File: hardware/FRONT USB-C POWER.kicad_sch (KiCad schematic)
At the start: 0 parts

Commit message: working on adujustabel otpur for usbpd
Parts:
- added C20: CIN, symbol Device:C
- added C21, C22: 2uF2, symbol Device:C
- added C23, C24, C27, C28, C29, C30, C33: C, symbol Device:C
- added C25: COUT2, symbol Device:C
- added C26: COUT1, symbol Device:C
- added C31, C32: 1uF, symbol Device:C
- added C34: 470nF, symbol Device:C
- added D2, D3: D_Shockley, symbol Device:D_Shockley
- added L3, L4: L, symbol Device:L
- added Q3, Q4, Q5, Q6: Q_NMOS_GDS, symbol Device:Q_NMOS_GDS
- added R13: RHO1, symbol Device:R
- added R14: RHO2, symbol Device:R
- added R15, R16, R17, R18: R, symbol Device:R
- added R19: 10K, symbol Device:R
- added R21, R22: 100K, symbol Device:R
- added R23: 470R, symbol Device:R
- added Uw: ~, symbol CARTHING:LM5143-Q1
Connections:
- new net: C21.1, C22.1, D2.2 (A), D3.2 (A), Uw.15 (VCC), Uw.16 (VCC)
- new net: C32.2, Uw.1 (SS2)
- new net: C24.2, L3.1, Q5.3 (S), Q6.2 (D), Uw.10 (SW2)
- new net: C24.1, D3.1 (K), Uw.11 (HB2)
- new net: Q6.1 (G), Uw.12 (LOL2), Uw.13 (LO2)
- new net: Q4.1 (G), Uw.18 (LO1), Uw.19 (LOL1)
- new net: C30.1, R17.1, Uw.2 (COMP2)
- new net: C23.2, D2.1 (K), Uw.20 (HB1)
- new net: C23.1, L4.2, Q3.3 (S), Q4.2 (D), Uw.21 (SW1)
- new net: R13.2, Uw.22 (HO1)
- new net: Q3.1 (G), R13.1, Uw.23 (HOL1)
- new net: L4.1, R15.2, Uw.27 (CS1)
- new net: C28.2, R18.2, Uw.29 (COMP1)
- new net: C31.2, Uw.30 (SS1)
- new net: C33.2, Uw.32 (RES)
- new net: C34.2, Uw.36 (VDDA), Uw.38 (DITH)
- new net: R19.1, Uw.37 (RT)
- new net: L3.2, R16.1, Uw.4 (CS2)
- new net: Q5.1 (G), R14.2, Uw.8 (HOL2)
- new net: R14.1, Uw.9 (HO2)
- new net: C29.1, R17.2
- new net: R19.2, R23.1
- new net: C27.2, R18.1
- new net +21V: C20.2, Q3.2 (D), Q5.2 (D), Uw.25 (VIN)
- new net +3V3: R21.2, R22.1
- new net +5V: Uw.6 (VCCX)
- new net B_SUB-C_BUCK_P-GOOD: R21.1, Uw.7 (PG2)
- new net B_USB-C_BUCK_EN: Uw.40 (EN2)
- new net B_USB-C_BUCK_FB: Uw.3 (FB2)
- new net B_USB-C_BUCK_OUT: C25.1, R16.2, Uw.5 (VOUT2)
- new net F_SUB-C_BUCK_P-GOOD: R22.2, Uw.24 (PG1)
- new net F_USB-C_BUCK_EN: Uw.31 (EN1)
- new net F_USB-C_BUCK_FB: Uw.28 (FB1)
- new net F_USB-C_BUCK_OUT: C26.1, R15.1, Uw.26 (VOUT1)
- new net GND: C20.1, C21.2, C22.2, C25.2, C26.2, C27.1, C28.1, C29.2, C30.2, C31.1, C32.1, C33.1, C34.1, Q4.3 (S), Q6.3 (S), R23.2, Uw.14 (PGND2), Uw.17 (PGND1), Uw.35 (AGND), Uw.EP
- new net USB-C_BUCK_CLK_IN: Uw.33 (DEMB)
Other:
- added sheet F_AND_B_VOUT_FEEDBACK_NETWORKS (F_AND_B_VOUT_FEEDBACK_NETWORKS.kicad_sch)
- note added: "2.1 MHz SW FREQ"
- note added: "CANT LEVE EN PINS FLOATING"

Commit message: making hardware progress
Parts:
- removed L3, L4: L, symbol Device:L
- added L1 (x2): IHLP2525CZER2R2M01, symbol Device:L
- added R51: 0R, symbol Device:R
- C20: renamed from C26; value COUT1 -> 4.7uF
- C21: renamed from C27; value C -> 4.7uF
- C22: renamed from C28; value C -> 18pF
- C24: renamed from C33; value C -> 470nF
- C25: renamed from C23; value C -> 0.1uF
- C26: renamed from C20; value CIN -> 50uF
- C30: renamed from C24; value C -> 0.1uF
- C32: renamed from C30; value C -> 18pF
- C33: renamed from C29; value C -> 4.7uF
- C34: renamed from C25; value COUT2 -> 4.7uF
- Q3, Q4, Q5, Q6: value Q_NMOS_GDS -> PMPB11EN,115
- R14: renamed from R18; value R -> 5.9K
- R15: value R -> 10mR
- R22: renamed from R16; value R -> 10mR
- R23: renamed from R17; value R -> 5.9K
- renumbered C31 to C23, C22 to C27, C34 to C28, C21 to C29, C32 to C31, R22 to R16, R13 to R17, R19 to R18, R14 to R19, R23 to R20, Uw to U6
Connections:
- net GND: now also U6.34 (MODE), R51.2
- net USB-C_BUCK_CLK_IN: now also R51.1
- net at C30.2, Q5.3 (S), Q6.2 (D)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: now also L1.1
- net at C25.1, Q3.3 (S), Q4.2 (D)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: now also L1.2
- net F_USB-C_CSN: now reaches R15.2, U6.27 (CS1)
- net F_USB-C_CSN: now also L1.1
- net B_USB-C_CSN: now reaches R22.1, U6.4 (CS2)
- net B_USB-C_CSN: now also L1.2
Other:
- note added: "2.2uH"
- moved on the sheet: C25, D2

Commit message: working on hardware
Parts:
- C24: renamed from C20; footprint (none) -> Capacitor_SMD:C_0603_1608Metric
- C25: renamed from C21; footprint (none) -> Capacitor_SMD:C_0603_1608Metric
- C26: renamed from C22; footprint (none) -> Capacitor_SMD:C_0603_1608Metric
- C27: renamed from C23; footprint (none) -> Capacitor_SMD:C_0603_1608Metric
- C28: renamed from C24; footprint (none) -> Capacitor_SMD:C_0805_2012Metric
- C29: renamed from C25; footprint (none) -> Capacitor_SMD:C_0603_1608Metric
- C30: renamed from C26; footprint (none) -> Capacitor_SMD:C_0603_1608Metric
- C31: renamed from C27; value 2uF2 -> 2.2uF; footprint (none) -> Capacitor_SMD:C_0603_1608Metric
- C32: renamed from C28; footprint (none) -> Capacitor_SMD:C_0805_2012Metric
- C33: renamed from C29; value 2uF2 -> 2.2uF; footprint (none) -> Capacitor_SMD:C_0603_1608Metric
- C34: renamed from C30; footprint (none) -> Capacitor_SMD:C_0603_1608Metric
- C35: renamed from C31; footprint (none) -> Capacitor_SMD:C_0603_1608Metric
- C36: renamed from C32; footprint (none) -> Capacitor_SMD:C_0603_1608Metric
- C37: renamed from C33; footprint (none) -> Capacitor_SMD:C_0603_1608Metric
- C38: renamed from C34; footprint (none) -> Capacitor_SMD:C_0603_1608Metric
- D3: renamed from D2; footprint (none) -> Diode_SMD:D_SMA
- D4: renamed from D3; footprint (none) -> Diode_SMD:D_SMA
- Q3, Q4, Q5, Q6: footprint (none) -> CARTHING:TRANS_PMPB11EN_115
- renumbered R14 to R17, R15 to R18, R16 to R19, R17 to R20, R51 to R21, R18 to R22, R19 to R23, R20 to R24, R21 to R25, R22 to R26, R23 to R27, U6 to U7

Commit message: working assighning footprints still
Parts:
- added TP8: TestPoint, TestPoint:TestPoint_Pad_D1.0mm, symbol Connector:TestPoint
- R17, R19, R20, R21, R22, R23, R24, R25, R27: footprint (none) -> Resistor_SMD:R_0603_1608Metric
- R18, R26: footprint (none) -> Resistor_SMD:R_1206_3216Metric
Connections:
- net at U7.39 (SYNCOUT): now also TP8.1
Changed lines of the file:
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@@
     (stroke (width 0) (type default))
   )
-  (wire (pts (xy 163.83 119.38) (xy 163.83 135.89))
+  (wire (pts (xy 170.18 119.38) (xy 170.18 135.89))
     (stroke (width 0) (type default))
   )
@@
     (stroke (width 0) (type default))
   )
-  (wire (pts (xy 158.75 119.38) (xy 163.83 119.38))
+  (wire (pts (xy 158.75 119.38) (xy 170.18 119.38))
     (stroke (width 0) (type default))
   )
@@
     (stroke (width 0) (type default))
   )
-  (wire (pts (xy 163.83 135.89) (xy 143.51 135.89))
+  (wire (pts (xy 143.51 135.89) (xy 170.18 135.89))
     (stroke (width 0) (type default))
   )
@@
     (stroke (width 0) (type default))
   )
-  (text "2.1 MHz SW FREQ\n" (at 166.37 137.16 0)
+  (text "2.1 MHz SW FREQ\n" (at 172.72 137.16 0)
     (effects (font (size 1.27 1.27)) (justify left bottom))
   )
@@
       (effects (font (size 1.27 1.27)))
     )
-    (property "Footprint" "" (at 224.79 107.188 90)
+    (property "Footprint" "Resistor_SMD:R_0603_1608Metric" (at 224.79 107.188 90)
       (effects (font (size 1.27 1.27)) hide)
     )
@@
       (effects (font (size 1.27 1.27)))
     )
-    (property "Footprint" "" (at 58.42 74.168 90)
+    (property "Footprint" "Resistor_SMD:R_1206_3216Metric" (at 58.42 74.168 90)
       (effects (font (size 1.27 1.27)) hide)
     )
@@
       (effects (font (size 1.27 1.27)))
     )
-    (property "Footprint" "" (at 115.57 131.318 90)
+    (property "Footprint" "Resistor_SMD:R_0603_1608Metric" (at 115.57 131.318 90)
       (effects (font (size 1.27 1.27)) hide)
     )
@@
       (effects (font (size 1.27 1.27)))
     )
-    (property "Footprint" "" (at 223.52 75.438 90)
+    (property "Footprint" "Resistor_SMD:R_1206_3216Metric" (at 223.52 75.438 90)
       (effects (font (size 1.27 1.27)) hide)
     )
@@
     )
   )
+  (symbol (lib_id "Connector:TestPoint") (at 158.75 121.92 180) (unit 1)
+    (in_bom yes) (on_board yes) (dnp no) (fields_autoplaced)
+    (property "Reference" "TP8" (at 160.147 124.5783 0)
+      (effects (font (size 1.27 1.27)) (justify right))
+    )
+    (property "Value" "TestPoint" (at 160.147 126.4993 0)
+      (effects (font (size 1.27 1.27)) (justify right))
+    )
+    (property "Footprint" "TestPoint:TestPoint_Pad_D1.0mm" (at 153.67 121.92 0)
+      (effects (font (size 1.27 1.27)) hide)
+    )
+    (property "Datasheet" "~" (at 153.67 121.92 0)
+      (effects (font (size 1.27 1.27)) hide)
+    )
+    (pin "1")
+    (instances
+      (project "usbc-car-module"
+        (path "/fae025e9-99c5-40c1-af6f-99dc1edbfa43/91b561d6-4186-4f6f-8a2c-57c2c305f210"
+          (reference "TP8") (unit 1)
+        )
+      )
+    )
+  )
   (symbol (lib_id "Device:R") (at 204.47 114.3 90) (unit 1)
     (in_bom yes) (on_board yes) (dnp no) (fields_autoplaced)
@@
       (effects (font (size 1.27 1.27)))
     )
-    (property "Footprint" "" (at 204.47 116.078 90)
+    (property "Footprint" "Resistor_SMD:R_0603_1608Metric" (at 204.47 116.078 90)
       (effects (font (size 1.27 1.27)) hide)
     )
@@
       (effects (font (size 1.27 1.27)))
     )
-    (property "Footprint" "" (at 168.91 72.898 90)
+    (property "Footprint" "Resistor_SMD:R_0603_1608Metric" (at 168.91 72.898 90)
       (effects (font (size 1.27 1.27)) hide)
     )
@@
       (effects (font (size 1.27 1.27)))
     )
-    (property "Footprint" "" (at 111.76 72.898 90)
+    (property "Footprint" "Resistor_SMD:R_0603_1608Metric" (at 111.76 72.898 90)
       (effects (font (size 1.27 1.27)) hide)
     )
@@
       (effects (font (size 1.27 1.27)))
     )
-    (property "Footprint" "" (at 165.1 118.618 90)
+    (property "Footprint" "Resistor_SMD:R_0603_1608Metric" (at 165.1 118.618 90)
       (effects (font (size 1.27 1.27)) hide)
     )
@@
       (effects (font (size 1.27 1.27)))
     )
-    (property "Footprint" "" (at 173.99 118.618 90)
+    (property "Footprint" "Resistor_SMD:R_0603_1608Metric" (at 173.99 118.618 90)
       (effects (font (size 1.27 1.27)) hide)
     )
@@
       (effects (font (size 1.27 1.27)))
     )
-    (property "Footprint" "" (at 57.15 108.458 90)
+    (property "Footprint" "Resistor_SMD:R_0603_1608Metric" (at 57.15 108.458 90)
       (effects (font (size 1.27 1.27)) hide)
     )
@@
       (effects (font (size 1.27 1.27)))
     )
-    (property "Footprint" "" (at 78.74 116.078 90)
-      (effects (font (size 1.27 1.27)) hide)
-    )
+    (property "Footprint" "Resistor_SMD:R_0603_1608Metric" (at 78.74 116.078 90)
+      (effects (font (size 1.27 1.27)) hide)
+    )

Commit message: FINALY starting the pcb
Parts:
- L1: footprint (none) -> CARTHING:IND25X25CZ
- U7: footprint (none) -> CARTHING:LM5143
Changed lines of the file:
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@@
       (effects (font (size 1.27 1.27)))
     )
-    (property "Footprint" "" (at 149.86 76.2 0)
+    (property "Footprint" "CARTHING:LM5143" (at 149.86 76.2 0)
       (effects (font (size 1.27 1.27)) hide)
     )
@@
       (effects (font (size 1.27 1.27)))
     )
-    (property "Footprint" "" (at 210.82 73.66 0)
+    (property "Footprint" "CARTHING:IND25X25CZ" (at 210.82 73.66 0)
       (effects (font (size 1.27 1.27)) hide)
     )
@@
       (effects (font (size 1.27 1.27)))
     )
-    (property "Footprint" "" (at 71.12 72.39 0)
-      (effects (font (size 1.27 1.27)) hide)
-    )
+    (property "Footprint" "CARTHING:IND25X25CZ" (at 71.12 72.39 0)
+      (effects (font (size 1.27 1.27)) hide)
+    )

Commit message: coldent sleep so came back and did somre routing
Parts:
- R20, R23: now not fitted
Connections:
- net +21V: now also Q3.1 (D), Q3.5 (D), Q3.6 (D), Q3.7 (D), Q5.1 (D), Q5.5 (D), Q5.6 (D), Q5.7 (D)
- net GND: now also Q4.4 (S), Q4.8 (S), Q6.4 (S), Q6.8 (S), U7.41 (EP); no longer Q4.3 (S), Q6.3 (S), U7.EP
- net at C34.2, L1.1, Q6.2 (D)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: now also Q5.4 (S), Q5.8 (S), Q6.1 (D), Q6.5 (D), Q6.6 (D), Q6.7 (D); no longer Q5.3 (S)
- net at U7.12 (LOL2), U7.13 (LO2): now also Q6.3 (G); no longer Q6.1 (G)
- net at U7.18 (LO1), U7.19 (LOL1): now also Q4.3 (G); no longer Q4.1 (G)
- net at C29.1, L1.2, Q4.2 (D)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: now also Q3.4 (S), Q3.8 (S), Q4.1 (D), Q4.5 (D), Q4.6 (D), Q4.7 (D); no longer Q3.3 (S)
- net at R20.1, U7.23 (HOL1): now also Q3.3 (G); no longer Q3.1 (G)
- net at R23.2, U7.8 (HOL2): now also Q5.3 (G); no longer Q5.1 (G)

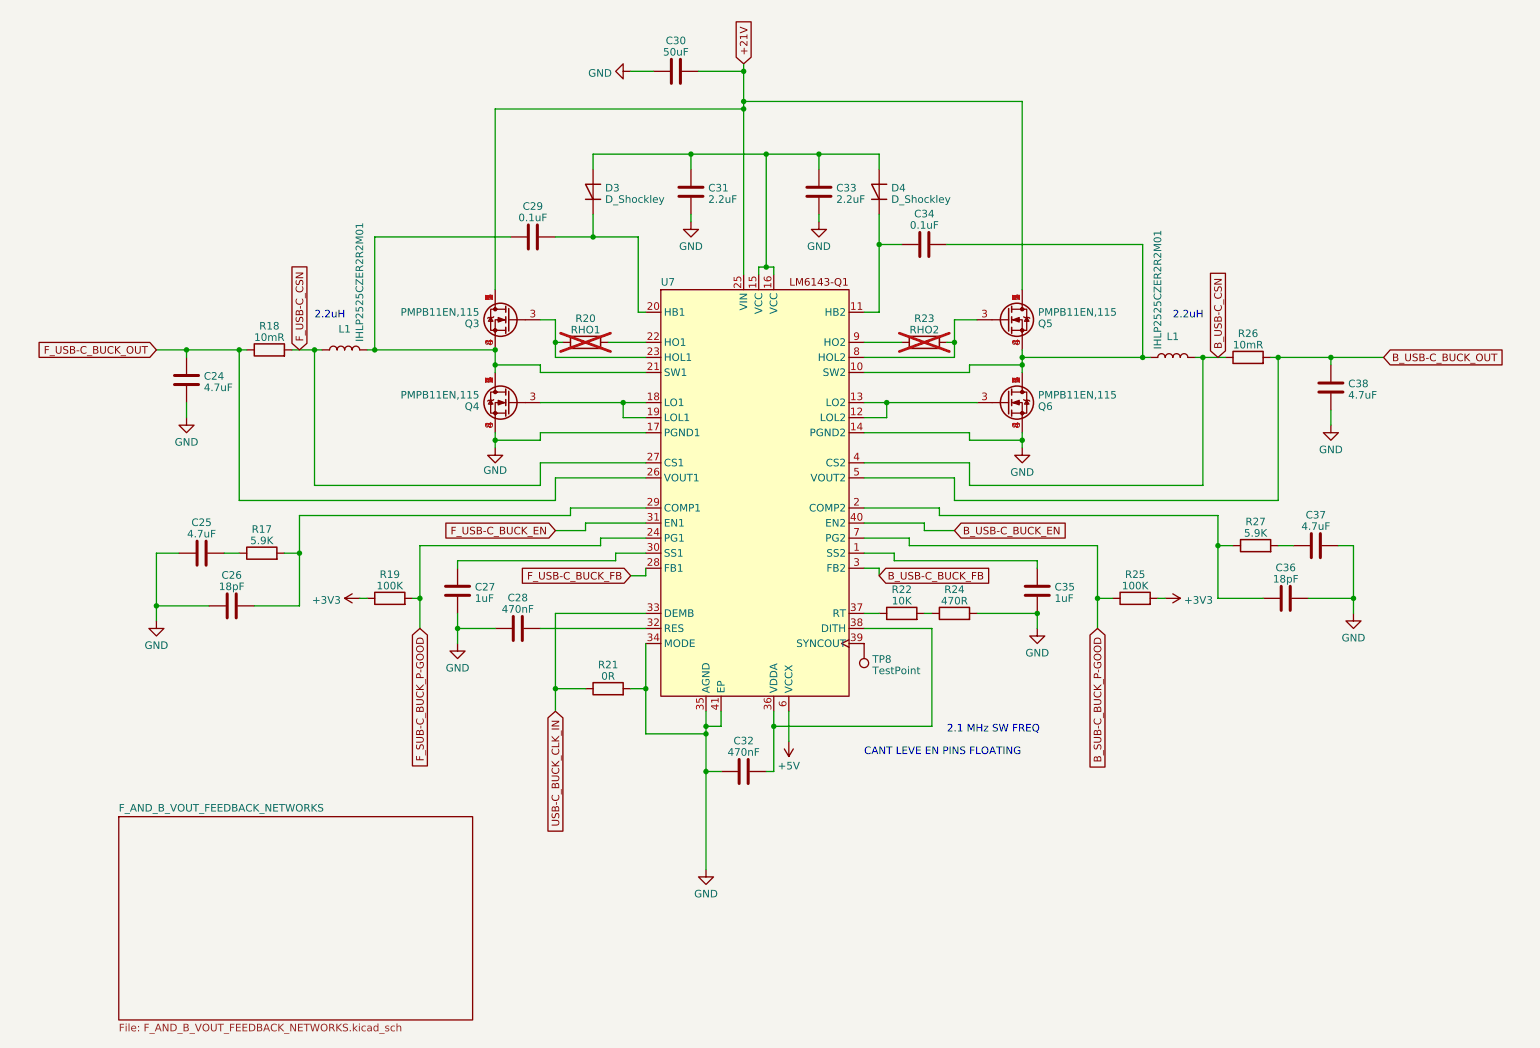
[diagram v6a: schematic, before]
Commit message: working on routing still  finnished psu section
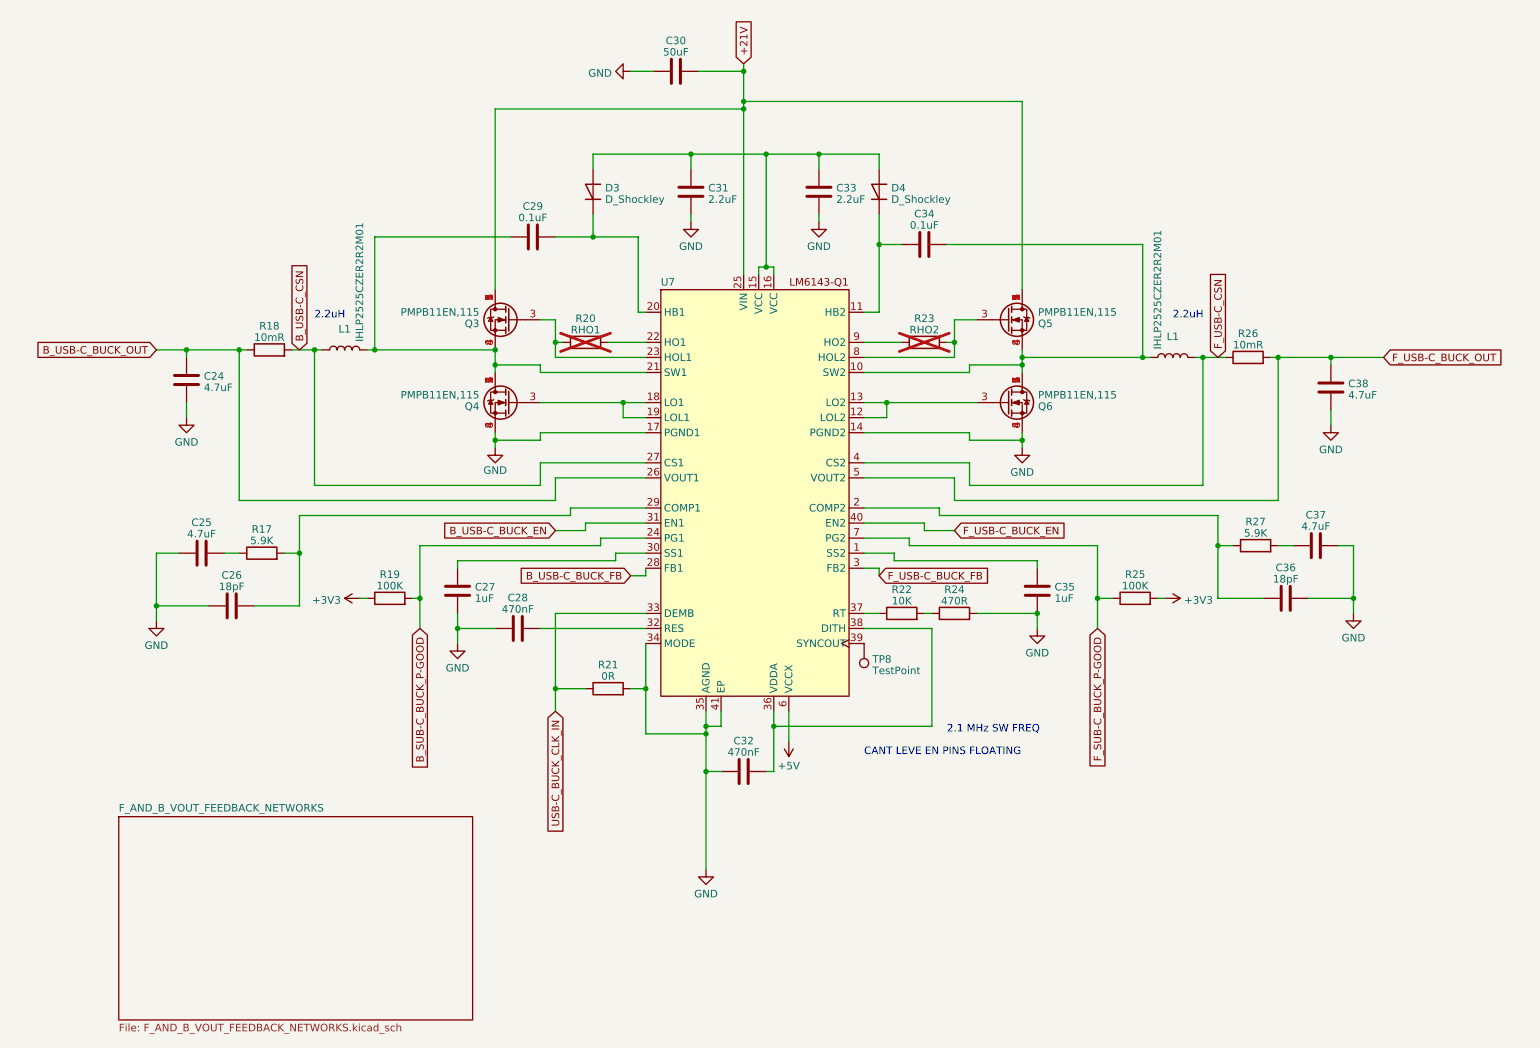
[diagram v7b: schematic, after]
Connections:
- net B_SUB-C_BUCK_P-GOOD: now also R19.2, U7.24 (PG1); no longer R25.1, U7.7 (PG2)
- net B_USB-C_BUCK_EN: now also U7.31 (EN1); no longer U7.40 (EN2)
- net B_USB-C_BUCK_FB: now also U7.28 (FB1); no longer U7.3 (FB2)
- net B_USB-C_BUCK_OUT: now also C24.1, R18.1, U7.26 (VOUT1); no longer C38.1, R26.2, U7.5 (VOUT2)
- net B_USB-C_CSN: now also L1.1, R18.2, U7.27 (CS1); no longer L1.2, R26.1, U7.4 (CS2)
- net F_SUB-C_BUCK_P-GOOD: now also R25.1, U7.7 (PG2); no longer R19.2, U7.24 (PG1)
- net F_USB-C_BUCK_EN: now also U7.40 (EN2); no longer U7.31 (EN1)
- net F_USB-C_BUCK_FB: now also U7.3 (FB2); no longer U7.28 (FB1)
- net F_USB-C_BUCK_OUT: now also C38.1, R26.2, U7.5 (VOUT2); no longer C24.1, R18.1, U7.26 (VOUT1)
- net F_USB-C_CSN: now also L1.2, R26.1, U7.4 (CS2); no longer L1.1, R18.2, U7.27 (CS1)
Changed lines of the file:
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@@
     )
   )
-  (global_label "B_USB-C_CSN" (shape input) (at 218.44 73.66 90) (fields_autoplaced)
+  (global_label "F_USB-C_CSN" (shape input) (at 218.44 73.66 90) (fields_autoplaced)
     (effects (font (size 1.27 1.27)) (justify left))
     (property "Intersheetrefs" "${INTERSHEET_REFS}" (at 218.44 57.0866 90)
@@
     )
   )
-  (global_label "B_USB-C_BUCK_EN" (shape input) (at 173.99 102.87 0) (fields_autoplaced)
+  (global_label "F_USB-C_BUCK_EN" (shape input) (at 173.99 102.87 0) (fields_autoplaced)
     (effects (font (size 1.27 1.27)) (justify left))
     (property "Intersheetrefs" "${INTERSHEET_REFS}" (at 198.9696 102.87 0)
@@
     )
   )
-  (global_label "F_USB-C_BUCK_EN" (shape input) (at 106.68 102.87 180) (fields_autoplaced)
+  (global_label "B_USB-C_BUCK_EN" (shape input) (at 106.68 102.87 180) (fields_autoplaced)
     (effects (font (size 1.27 1.27)) (justify right))
     (property "Intersheetrefs" "${INTERSHEET_REFS}" (at 80.6118 102.87 0)
@@
     )
   )
-  (global_label "F_USB-C_BUCK_OUT" (shape input) (at 39.37 72.39 180) (fields_autoplaced)
+  (global_label "B_USB-C_BUCK_OUT" (shape input) (at 39.37 72.39 180) (fields_autoplaced)
     (effects (font (size 1.27 1.27)) (justify right))
     (property "Intersheetrefs" "${INTERSHEET_REFS}" (at 12.1527 72.39 0)
@@
     )
   )
-  (global_label "F_SUB-C_BUCK_P-GOOD" (shape input) (at 83.82 119.38 270) (fields_autoplaced)
+  (global_label "B_SUB-C_BUCK_P-GOOD" (shape input) (at 83.82 119.38 270) (fields_autoplaced)
     (effects (font (size 1.27 1.27)) (justify right))
     (property "Intersheetrefs" "${INTERSHEET_REFS}" (at 83.82 151.0121 90)
@@
     )
   )
-  (global_label "F_USB-C_CSN" (shape input) (at 63.5 72.39 90) (fields_autoplaced)
+  (global_label "B_USB-C_CSN" (shape input) (at 63.5 72.39 90) (fields_autoplaced)
     (effects (font (size 1.27 1.27)) (justify left))
     (property "Intersheetrefs" "${INTERSHEET_REFS}" (at 63.5 55.998 90)
@@
     )
   )
-  (global_label "B_USB-C_BUCK_FB" (shape input) (at 161.29 110.49 0) (fields_autoplaced)
+  (global_label "F_USB-C_BUCK_FB" (shape input) (at 161.29 110.49 0) (fields_autoplaced)
     (effects (font (size 1.27 1.27)) (justify left))
     (property "Intersheetrefs" "${INTERSHEET_REFS}" (at 182.5201 110.49 0)
@@
     )
   )
-  (global_label "B_SUB-C_BUCK_P-GOOD" (shape input) (at 198.12 119.38 270) (fields_autoplaced)
+  (global_label "F_SUB-C_BUCK_P-GOOD" (shape input) (at 198.12 119.38 270) (fields_autoplaced)
     (effects (font (size 1.27 1.27)) (justify right))
     (property "Intersheetrefs" "${INTERSHEET_REFS}" (at 198.12 149.9235 90)
@@
     )
   )
-  (global_label "F_USB-C_BUCK_FB" (shape input) (at 119.38 110.49 180) (fields_autoplaced)
+  (global_label "B_USB-C_BUCK_FB" (shape input) (at 119.38 110.49 180) (fields_autoplaced)
     (effects (font (size 1.27 1.27)) (justify right))
     (property "Intersheetrefs" "${INTERSHEET_REFS}" (at 98.3313 110.49 0)
@@
     )
   )
-  (global_label "B_USB-C_BUCK_OUT" (shape input) (at 246.38 73.66 0) (fields_autoplaced)
+  (global_label "F_USB-C_BUCK_OUT" (shape input) (at 246.38 73.66 0) (fields_autoplaced)
     (effects (font (size 1.27 1.27)) (justify left))
     (property "Intersheetrefs" "${INTERSHEET_REFS}" (at 272.5087 73.66 0)

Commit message: finaliseing pcb layout will come back later for a fresh look
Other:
- company: (none) -> MICK MAKE
- title: (none) -> 200W USB PD 3.1 HUB
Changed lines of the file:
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@@
 (kicad_sch (version 20230121) (generator eeschema)
   (paper "A4")
+  (title_block
+    (title "200W USB PD 3.1 HUB")
+    (date "2023-10-03")
+    (rev "A")
+    (company "MICK MAKE")
+    (comment 1 "THIS IS A 2X 100W USB PD SOURCE ")
+    (comment 2 "HUB USB SPEC 3.1")
+    (comment 3 "TOTAL SYSTEM POWER IS ~275w")
+  )
   (junction (at 187.96 116.84) (diameter 0) (color 0 0 0 0)
   )
